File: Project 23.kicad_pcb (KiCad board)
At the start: 2 copper layers, 62 x 42 mm, 65 parts, among them J11 SRX 1, J12 SRX 2, J13 SWD, J21 BATT +, J22 BATT-, J61 USB_Micro, J71 Micro_SD_Card_Det, SW11 UI_Btn, SW12 PWR_BTN, U1 STM32F103C8T7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

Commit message: Power Routed
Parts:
- moved F11 13.2 mm to (91.2, 77.5)
- moved TP32 8.09 mm to (85.1, 80.0)
- moved TP31 7.88 mm to (87.6, 80.0)
- moved TP41 7.67 mm to (90.2, 80.0)
- moved F12 7.48 mm to (84.9, 77.5)
- moved TP75 7.46 mm to (92.7, 80.0)
- moved RN12 1.60 mm to (75.9, 69.0)
- moved RN11 1.52 mm to (72.1, 69.0)
- moved U2 1.37 mm to (84.2, 70.0)
- moved J12 1.27 mm to (74.9, 75.0)
- moved RN1 1.27 mm to (85.1, 63.2)
- moved R15 1.02 mm to (81.3, 66.3)
- moved L41 0.85 mm to (89.2, 71.8)
- moved D11 0.76 mm to (80.0, 62.0)
- moved R16 0.51 mm to (78.7, 66.3)
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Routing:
- net GND: track 91.3 -> 0.00 mm, vias 35 -> 0
- net /Power_Btn: track 45.3 -> 0.00 mm, vias 5 -> 0
- net /PWR_EN: track 41.3 -> 0.00 mm, vias 7 -> 0
- net /SCK2: track 36.8 -> 0.00 mm, vias 2 -> 0
- net /MISO2: track 35.6 -> 0.00 mm, vias 2 -> 0
- net /MOSI2: track 35.2 -> 0.00 mm, vias 2 -> 0
- net /SS2: track 34.9 -> 0.00 mm, vias 2 -> 0
- net /UI_Btn: track 33.2 -> 0.00 mm, vias 2 -> 0
- net Net-(J11-Pad8): track 32.8 -> 0.00 mm, vias 3 -> 0
- net /SD_CD: track 31.9 -> 0.00 mm, vias 4 -> 0
- net Net-(J11-Pad6): track 29.1 -> 0.00 mm, vias 5 -> 0
- net Net-(J11-Pad4): track 26.9 -> 0.00 mm, vias 2 -> 0
- net Net-(R41-Pad2): track 24.1 -> 0.00 mm, vias 2 -> 0
- net Net-(J11-Pad7): track 22.8 -> 0.00 mm, vias 3 -> 0
- net /Stat: track 34.3 -> 11.7 mm, vias 4 -> 0
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- removed copper zone on B.Cu, net GND
- removed copper zone on F.Cu, net GND
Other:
- net class Power: trace_width 0.22 -> 0.35; via_dia 0.6 -> 0.7; via_drill 0.4 -> 0.5

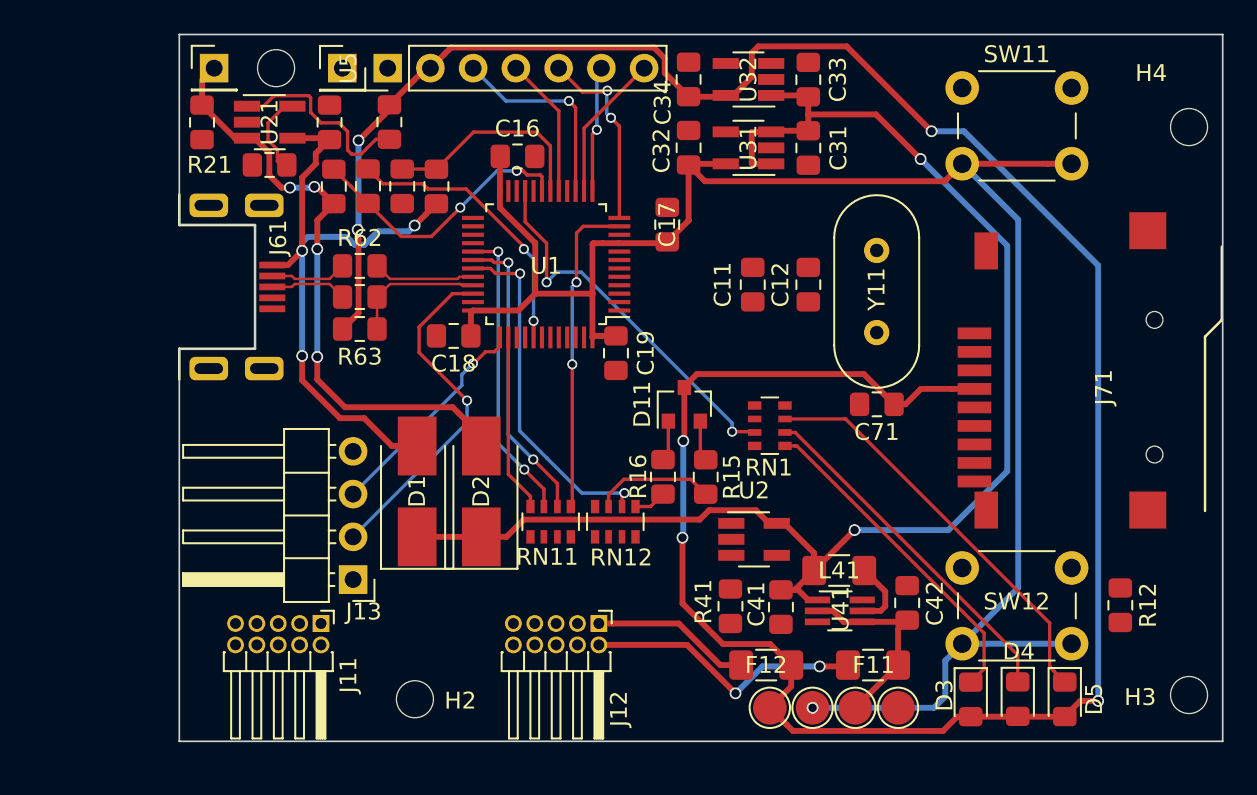
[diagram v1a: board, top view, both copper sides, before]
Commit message: Power lines routed
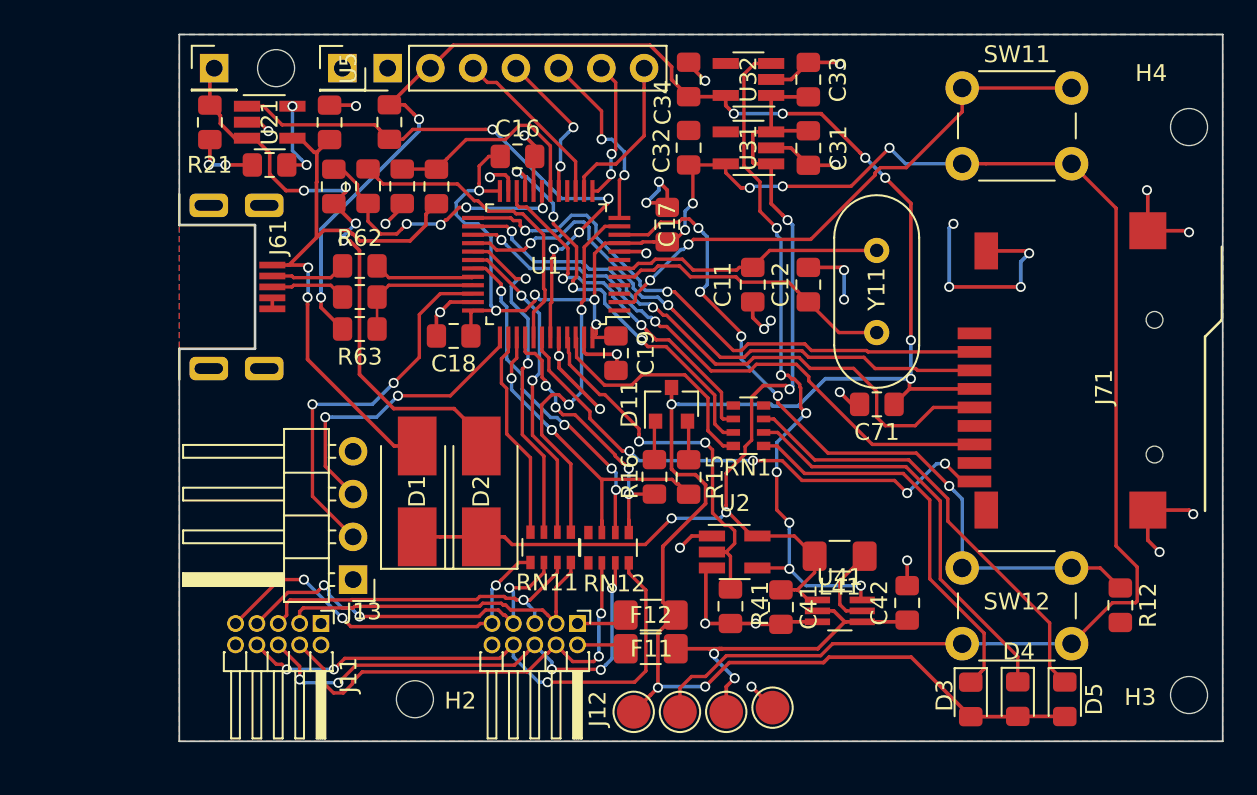
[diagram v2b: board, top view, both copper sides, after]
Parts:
- moved F11 13.2 mm to (78.0, 76.5)
- moved TP32 8.09 mm to (77.0, 80.2)
- moved TP31 7.88 mm to (79.8, 80.2)
- moved TP41 7.67 mm to (82.5, 80.2)
- moved F12 7.48 mm to (78.0, 74.5)
- moved TP75 7.46 mm to (85.2, 80.0)
- moved RN12 1.60 mm to (75.5, 70.5)
- moved RN11 1.52 mm to (72.1, 70.5)
- moved U2 1.37 mm to (83.0, 70.8)
- moved J12 1.27 mm to (73.7, 75.0)
- moved RN1 1.27 mm to (83.8, 63.2)
- moved R15 1.02 mm to (80.3, 66.3)
- moved L41 0.85 mm to (89.2, 71.0)
- moved D11 0.76 mm to (79.2, 62.0)
- moved R16 0.51 mm to (78.2, 66.3)
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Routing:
- net GND: track 0.00 -> 91.3 mm, vias 0 -> 35
- net /Power_Btn: track 0.00 -> 45.3 mm, vias 0 -> 5
- net /PWR_EN: track 0.00 -> 41.3 mm, vias 0 -> 7
- net /SCK2: track 0.00 -> 36.8 mm, vias 0 -> 2
- net /MISO2: track 0.00 -> 35.6 mm, vias 0 -> 2
- net /MOSI2: track 0.00 -> 35.2 mm, vias 0 -> 2
- net /SS2: track 0.00 -> 34.9 mm, vias 0 -> 2
- net /UI_Btn: track 0.00 -> 33.2 mm, vias 0 -> 2
- net Net-(J11-Pad8): track 0.00 -> 32.8 mm, vias 0 -> 3
- net /SD_CD: track 0.00 -> 31.9 mm, vias 0 -> 4
- net Net-(J11-Pad6): track 0.00 -> 29.1 mm, vias 0 -> 5
- net Net-(J11-Pad4): track 0.00 -> 26.9 mm, vias 0 -> 2
- net Net-(R41-Pad2): track 0.00 -> 24.1 mm, vias 0 -> 2
- net Net-(J11-Pad7): track 0.00 -> 22.8 mm, vias 0 -> 3
- net /Stat: track 11.7 -> 34.3 mm, vias 0 -> 4
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- added copper zone on B.Cu, net GND
- added copper zone on F.Cu, net GND
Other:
- net class Power: trace_width 0.35 -> 0.22; via_dia 0.7 -> 0.6; via_drill 0.5 -> 0.4

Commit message: Minor routing changes
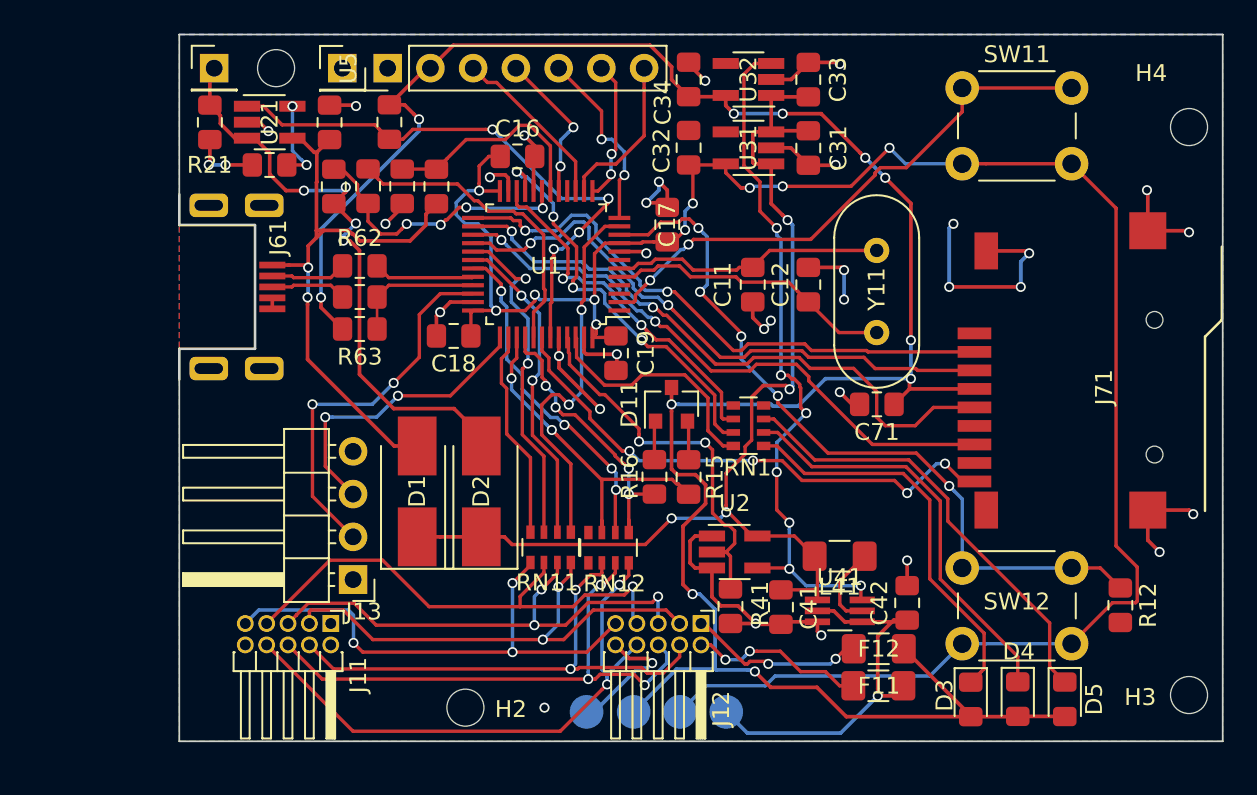
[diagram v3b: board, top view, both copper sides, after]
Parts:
- TP31, TP32, TP41, TP75: moved to B.Cu
- moved F11 13.7 mm to (91.5, 78.7)
- moved F12 13.7 mm to (91.6, 76.5)
- moved TP75 11.1 mm to (74.2, 80.2)
- moved J12 7.34 mm to (81.0, 75.0)
- moved H2 3.04 mm to (67.0, 80.0)
- moved J11 0.58 mm to (59.0, 75.0)
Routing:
- net Net-(J11-Pad3): track 20.6 -> 29.8 mm, vias 0 -> 2
- net Net-(J11-Pad5): track 20.7 -> 29.6 mm, vias 1 -> 3
- net GND: track 91.3 -> 99.6 mm
- net Net-(J11-Pad9): track 22.5 -> 30.8 mm
- net Net-(F12-Pad1): track 3.07 -> 10.8 mm, vias 0 -> 2
- net Net-(J11-Pad7): track 22.8 -> 30.5 mm, vias 3 -> 1
- net Net-(F11-Pad2): track 2.96 -> 10.5 mm, vias 0 -> 2
- net Net-(J11-Pad4): track 26.9 -> 31.3 mm
- net Net-(J11-Pad6): track 29.1 -> 33.3 mm, vias 5 -> 3
- net +3V3: track 135.4 -> 139.2 mm
- net +5V: track 21.1 -> 23.9 mm, vias 2 -> 1
- net Net-(J11-Pad8): track 32.8 -> 34.0 mm, vias 3 -> 2
- net VCC: track 65.2 -> 66.3 mm
- net /3V3SB: track 123.3 -> 122.5 mm

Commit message: Reworked USB Socket
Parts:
- removed H1: M2, MountingHole:MountingHole_2.2mm_M2
- added G***: LOGO, Project 23:goldfish, B.Cu at (100.0, 61.4)
- J61: value USB_Micro -> Molex 0476420001; footprint Project 23:microUsbSunken -> Project 23:Molex0476420001_UsbMicro
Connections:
- J11 pad 1: (no net) -> Net-(J11-Pad1)
- J11 pad 2: (no net) -> Net-(J11-Pad2)
- J13 pad 1: (no net) -> Net-(J13-Pad1)
- J71 pad 1: (no net) -> Net-(J71-Pad1)
- J71 pad 8: (no net) -> Net-(J71-Pad8)
- RN1 pad 1: (no net) -> Net-(RN1-Pad1)
- RN1 pad 8: (no net) -> Net-(RN1-Pad8)
- RN12 pad 1: (no net) -> Net-(RN12-Pad1)
- RN12 pad 8: (no net) -> Net-(RN12-Pad8)
- U1 pad 1: (no net) -> Net-(U1-Pad1)
- U1 pad 16: (no net) -> /MISO
- U1 pad 3: (no net) -> Net-(U1-Pad3)
- U1 pad 4: (no net) -> Net-(U1-Pad4)
- U1 pad 7: (no net) -> /Reset
- U31 pad 4: (no net) -> Net-(U31-Pad4)
- U32 pad 4: (no net) -> Net-(U32-Pad4)
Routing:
- net /D-: track 6.01 -> 0.00 mm
- net /D+: track 7.89 -> 1.90 mm
- net /P+: track 4.51 -> 0.14 mm
- net /P-: track 4.51 -> 0.14 mm
- net GND: track 99.6 -> 102.0 mm, vias 35 -> 36
- net Net-(R21-Pad1): track 5.01 -> 5.85 mm
- net VBUS: track 35.5 -> 36.2 mm
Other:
- outline, holes or cut-outs redrawn
- net class Diff Pair: clearance 0.152 -> 0.14; trace_width 0.152 -> 0.14
- rule trace_min: 0.152 -> 0.14

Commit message: Added USB traces
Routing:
- net /D-: track 0.00 -> 6.01 mm
- net /D+: track 1.90 -> 7.89 mm
- net /P-: track 0.14 -> 3.37 mm
- net /P+: track 0.14 -> 3.37 mm
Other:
- net class Diff Pair: clearance 0.14 -> 0.152; trace_width 0.14 -> 0.152
- rule trace_min: 0.14 -> 0.152
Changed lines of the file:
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@@
-(kicad_pcb (version 20171130) (host pcbnew "(5.0.2)-1")
+(kicad_pcb (version 20171130) (host pcbnew "(5.0.0)")
   (general
     (thickness 1.6)
     (drawings 10)
-    (tracks 1204)
+    (tracks 1220)
     (zones 0)
     (modules 65)
@@
     (zone_clearance 0.508)
     (zone_45_only no)
-    (trace_min 0.14)
+    (trace_min 0.152)
     (segment_width 0.2)
     (edge_width 0.1)
@@
   )
   (net_class "Diff Pair" ""
-    (clearance 0.14)
-    (trace_width 0.14)
+    (clearance 0.152)
+    (trace_width 0.152)
     (via_dia 0.6)
     (via_drill 0.4)
@@
   (segment (start 59.098264 62.738) (end 58.674 62.738) (width 0.203) (layer B.Cu) (net 19))
   (segment (start 61.722 62.738) (end 59.098264 62.738) (width 0.203) (layer B.Cu) (net 19))
-  (segment (start 56.687501 55) (end 56.787501 54.9) (width 0.2) (layer F.Cu) (net 20))
-  (segment (start 56.687501 54.35) (end 56.787501 54.45) (width 0.2) (layer F.Cu) (net 21))
+  (segment (start 56.687501 55) (end 56.787501 54.9) (width 0.152) (layer F.Cu) (net 20))
+  (segment (start 59 54.9) (end 59.7 55.6) (width 0.2) (layer F.Cu) (net 20))
+  (segment (start 58.175001 54.9) (end 59 54.9) (width 0.2) (layer F.Cu) (net 20))
+  (segment (start 56.8 55) (end 58.075001 55) (width 0.2) (layer F.Cu) (net 20))
+  (segment (start 58.075001 55) (end 58.175001 54.9) (width 0.2) (layer F.Cu) (net 20))
+  (segment (start 56.687501 54.35) (end 56.787501 54.45) (width 0.152) (layer F.Cu) (net 21))
+  (segment (start 58.075001 54.35) (end 58.175001 54.45) (width 0.2) (layer F.Cu) (net 21))
+  (segment (start 56.8 54.35) (end 58.075001 54.35) (width 0.2) (layer F.Cu) (net 21))
+  (segment (start 58.175001 54.45) (end 59 54.45) (width 0.2) (layer F.Cu) (net 21))
+  (segment (start 59 54.45) (end 59.7 53.75) (width 0.2) (layer F.Cu) (net 21))
   (segment (start 104.729 71.7) (end 103.02 71.7) (width 0.203) (layer F.Cu) (net 22) (status 20))
   (segment (start 105.918 72.889) (end 104.729 71.7) (width 0.203) (layer F.Cu) (net 22) (status 10))
@@
   (segment (start 95.749988 66.82875) (end 93.79623 64.874992) (width 0.203) (layer F.Cu) (net 22))
   (segment (start 61.75 55.6) (end 61.75 57.5) (width 0.152) (layer F.Cu) (net 23) (status 30))
+  (segment (start 62.45 54.9) (end 67.4 54.9) (width 0.2) (layer F.Cu) (net 23))
+  (segment (start 67.4 54.9) (end 67.45 54.9) (width 0.2) (layer F.Cu) (net 23))
+  (segment (start 61.75 55.6) (end 62.45 54.9) (width 0.2) (layer F.Cu) (net 23))
+  (segment (start 62.45 54.45) (end 66.494998 54.45) (width 0.2) (layer F.Cu) (net 24))
+  (segment (start 66.519999 54.424999) (end 67.425001 54.424999) (width 0.2) (layer F.Cu) (net 24))
+  (segment (start 61.75 53.75) (end 62.45 54.45) (width 0.2) (layer F.Cu) (net 24))
+  (segment (start 67.425001 54.424999) (end 67.45 54.4) (width 0.2) (layer F.Cu) (net 24))
+  (segment (start 66.494998 54.45) (end 66.519999 54.424999) (width 0.2) (layer F.Cu) (net 24))
   (via (at 77.47 58.166) (size 0.6) (drill 0.4) (layers F.Cu B.Cu) (net 25))
   (segment (start 78.930433 58.54849) (end 81.815488 61.433545) (width 0.203) (layer F.Cu) (net 25))

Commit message: Updated SRX connectors
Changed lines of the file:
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@@
   (module "Project 23:Molex0476420001_UsbMicro" locked (layer F.Cu)
     (at 50 55 270)
-    (fp_text reference J61 (at 0 7.62 270) (layer F.SilkS)
+    (fp_text reference J61 (at 0 -3.15 270) (layer F.SilkS)
       (effects (font (size 1 1) (thickness 0.15)))
     )

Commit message: Update Project 23.kicad_pcb
Locked components
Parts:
- J11, J12: footprint Connector_PinHeader_1.27mm:PinHeader_2x05_P1.27mm_Horizontal -> Project 23:20021512-00010T4LF

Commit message: Created bom and regenerated gerber files
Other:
- rule solder_mask_min_width: 0.25 -> 0.11
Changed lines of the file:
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@@
     (pad_drill 1.1)
     (pad_to_mask_clearance 0.05)
-    (solder_mask_min_width 0.25)
+    (solder_mask_min_width 0.11)
     (aux_axis_origin 0 0)
     (visible_elements 7FFFFFFF)
